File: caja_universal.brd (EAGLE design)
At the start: 136.8 x 101.5 mm, 39 parts, among them IC1 AD711N, IC2 AD620N, IC3 TL084P, IC4 TL084P, IC5 AD711N

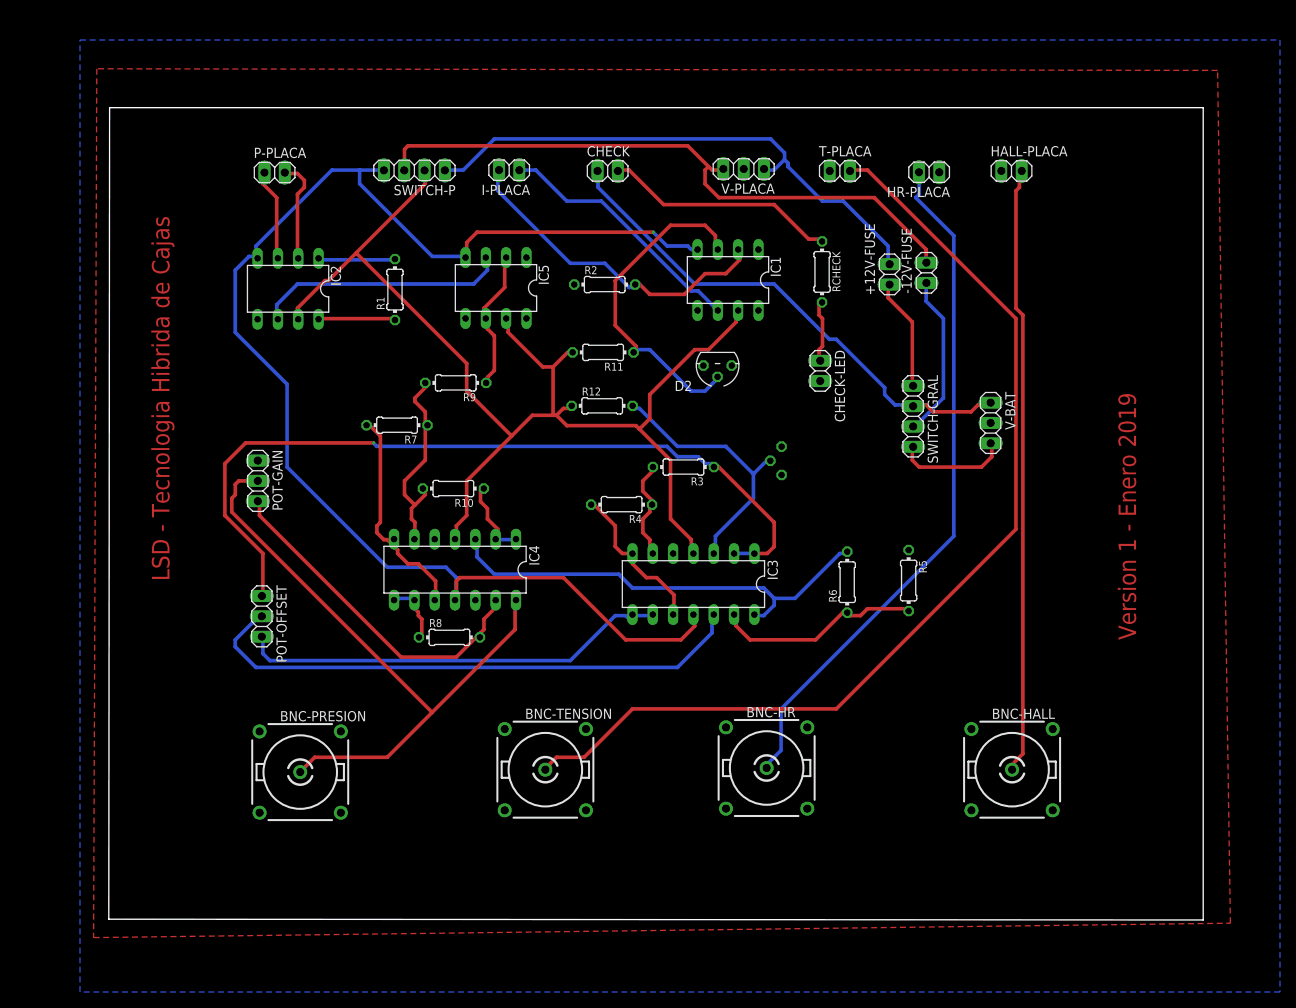
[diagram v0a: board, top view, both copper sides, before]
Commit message: Nuevo circuito de sense
Agrego circuito diseñado por Gonza para no tener que usar los cables de check
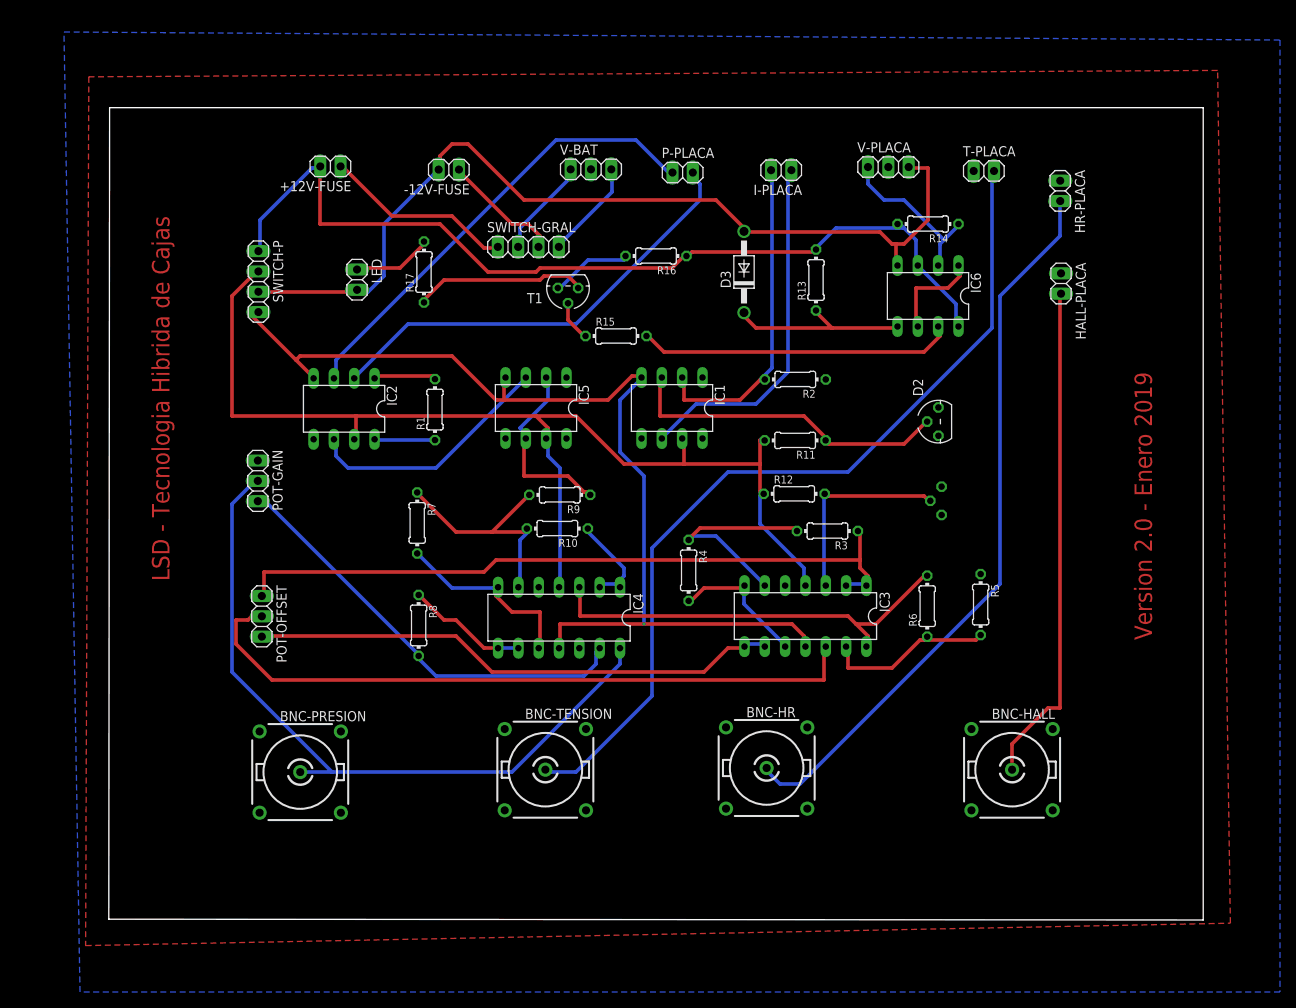
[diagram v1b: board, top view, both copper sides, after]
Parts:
- removed CHECK, CHECK-LED: (no value), pinhead:1X02
- removed RCHECK: 100k, resistor:0204/7
- added D3: BAT49, diode:DO41-10
- added IC6: AD826N, analog-devices:DIL08
- added LED: (no value), pinhead:1X02
- added R13, R15: 100k, resistor:0204/7
- added R14: 10, resistor:0204/7
- added R16, R17: 10k, resistor:0204/7
- added T1: 2N3904, transistor:TO92
- moved +12V-FUSE 71.2 mm to (9.30, 81.2), turned to 180 degrees
- moved -12V-FUSE 61.1 mm to (24.1, 80.8), turned to 180 degrees
- moved V-BAT 59.2 mm to (41.9, 80.8), turned to 0 degrees
- moved SWITCH-GRAL 52.6 mm to (34.0, 71.1), turned to 0 degrees
- moved P-PLACA 51.0 mm to (53.3, 80.4)
- moved I-PLACA 34.0 mm to (65.7, 80.7)
- moved D2 28.5 mm to (85.3, 49.3), turned to 90 degrees
- moved R2 26.6 mm to (67.4, 54.6), turned to 180 degrees
- moved R11 26.4 mm to (67.4, 47.0)
- moved R12 26.4 mm to (67.3, 40.3)
- moved SWITCH-P 23.9 mm to (0.30, 66.8), turned to 270 degrees
- moved D1 20.6 mm to (85.7, 39.4)
- moved R3 19.7 mm to (71.4, 35.6)
- moved R9 19.1 mm to (38.0, 40.1)
- moved V-PLACA 18.1 mm to (79.0, 81.1), turned to 0 degrees
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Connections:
- removed net N$1: CHECK-LED.1, RCHECK.2
- removed net N$2: CHECK.2, RCHECK.1
- new net +12VPLACA: IC6.2, R14.1, V-PLACA.1
- new net CHECK-LED: LED.1, R17.2
- new net N$17: R15.1, T1.2
- new net N$18: R16.2, T1.1
- new net N$19: R17.1, T1.3
- new net N$21: IC6.1, IC6.6
- new net N$23: D3.C, IC6.5, R13.1
- new net N$24: IC6.7, R15.2
- net +12V: now also IC6.3, IC6.8, R13.2, R14.2, R16.1; no longer V-PLACA.1
- net +12VBAT: no longer CHECK.1
- net -12V: now also D3.A, IC6.4, LED.2
- net 0V: no longer CHECK-LED.2
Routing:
- net +12VBAT: track 63.9 -> 12.4 mm
- net +12V: track 68.8 -> 115.7 mm
- net P+: track 11.6 -> 58.1 mm
- net P-: track 12.9 -> 56.3 mm
- net V-: track 170.7 -> 130.9 mm
- net N$24: track 0.00 -> 39.6 mm
- net -12V: track 79.0 -> 114.7 mm
- net N$2: track 29.3 -> 0.00 mm
- net N$23: track 0.00 -> 23.3 mm
- net N$19: track 0.00 -> 21.9 mm
- net +12VPLACA: track 0.00 -> 21.0 mm
- net TENSION: track 126.6 -> 109.5 mm
- net OFFSET: track 70.3 -> 86.1 mm
- net N$6: track 13.3 -> 26.8 mm
- net HALL: track 76.4 -> 62.9 mm
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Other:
- board text added: "Version 2.0 - Enero 2019"
- board text removed: "Version 1 - Enero 2019"

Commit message: Version 2.1
Smasheo todo para que los nombres y valores de todos los componentes queden visibles

Cambio los nombres de los integrados para que sean los que usamos
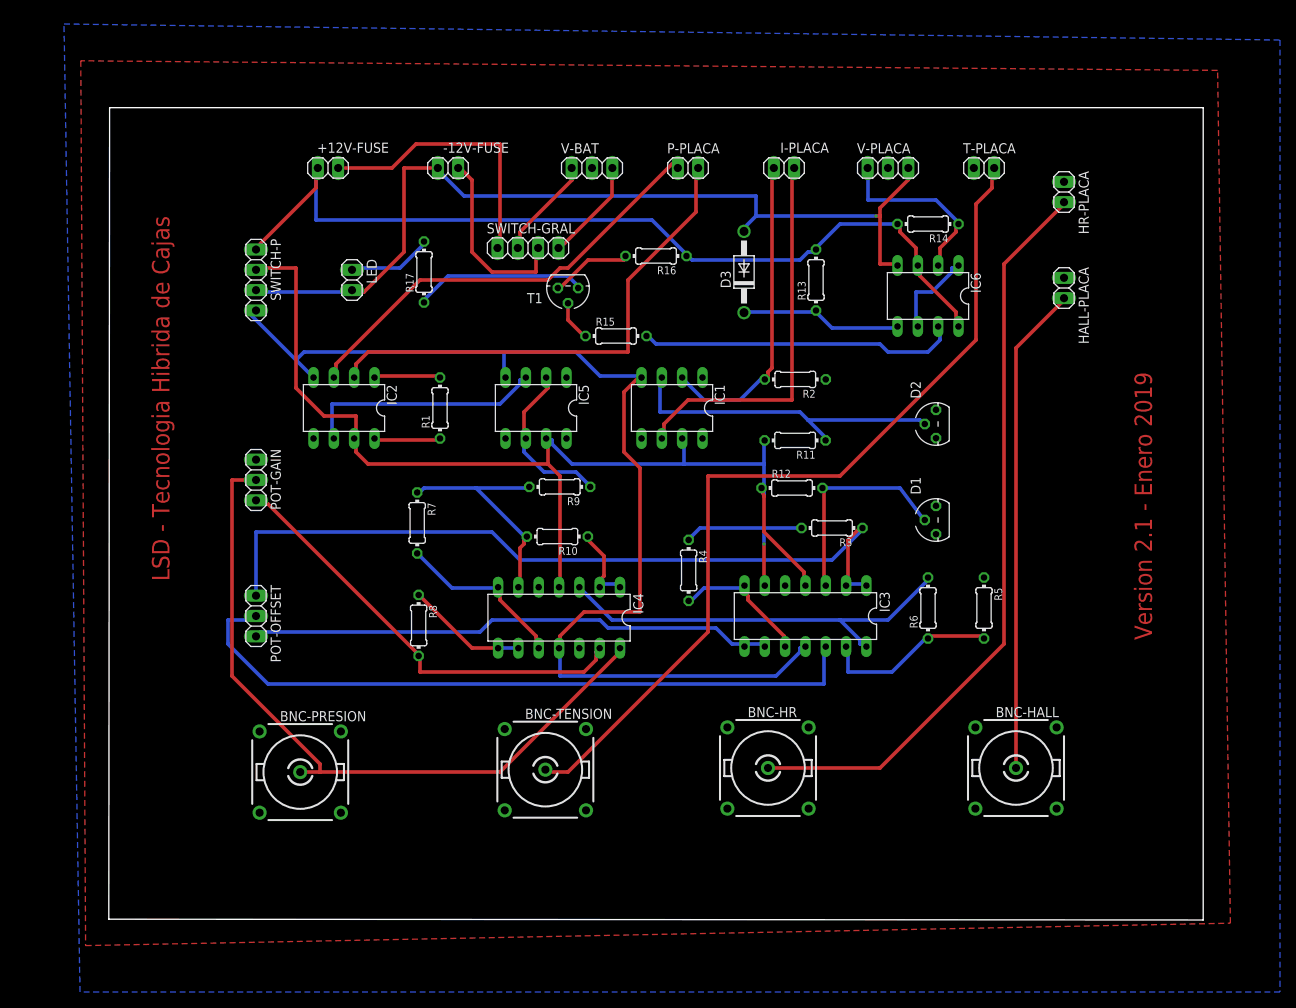
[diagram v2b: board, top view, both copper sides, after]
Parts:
- IC1, IC5: value AD711N -> NE5534
- IC6: value AD826N -> TL072
- moved D1 2.50 mm to (85.0, 37.0), flipped to the top, turned to 90 degrees
- moved R10 1.00 mm to (37.7, 34.9)
- moved R9 1.00 mm to (38.0, 41.1)
- moved P-PLACA 0.88 mm to (54.0, 81.0)
- moved R12 0.78 mm to (67.0, 41.0)
- moved POT-OFFSET 0.73 mm to (0.00, 25.0)
- moved R3 0.69 mm to (72.0, 36.0)
- moved HALL-PLACA 0.67 mm to (101.0, 66.0)
- moved R1 0.66 mm to (23.0, 51.0)
- moved LED 0.63 mm to (12.0, 67.0)
- moved R5 0.60 mm to (91.0, 26.0)
- moved BNC-HALL 0.53 mm to (95.0, 6.00)
- moved HR-PLACA 0.49 mm to (101.0, 78.0)
- moved I-PLACA 0.44 mm to (66.0, 81.0)
- moved D2 0.42 mm to (85.0, 49.0)
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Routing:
- net +12VFUSE: track 23.9 -> 34.8 mm
- net V-: track 130.9 -> 140.5 mm, vias 1 -> 0
- net 1.25V: track 88.5 -> 98.2 mm
- net -12VFUSE: track 15.0 -> 23.7 mm
- net P-: track 56.3 -> 63.2 mm
- net V+: track 138.8 -> 132.3 mm
- net N$6: track 26.8 -> 22.0 mm, vias 0 -> 1
- net +I: track 44.7 -> 48.4 mm
- net N$23: track 23.3 -> 20.4 mm
- net N$13: track 23.7 -> 20.9 mm
- net P+: track 58.1 -> 55.4 mm
- net N$9: track 13.2 -> 10.7 mm
- net +12VPLACA: track 21.0 -> 23.4 mm
- net N$14: track 24.2 -> 21.9 mm
- net HR: track 92.0 -> 94.3 mm
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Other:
- board text added: "Version 2.1 - Enero 2019"
- board text removed: "Version 2.0 - Enero 2019"

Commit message: Corregidos valores circuito sense, potenciometro gain y cambio de libreria conectores. Agrego tRestrict alrededor de conectores para que las vias salgan siempre de bottom
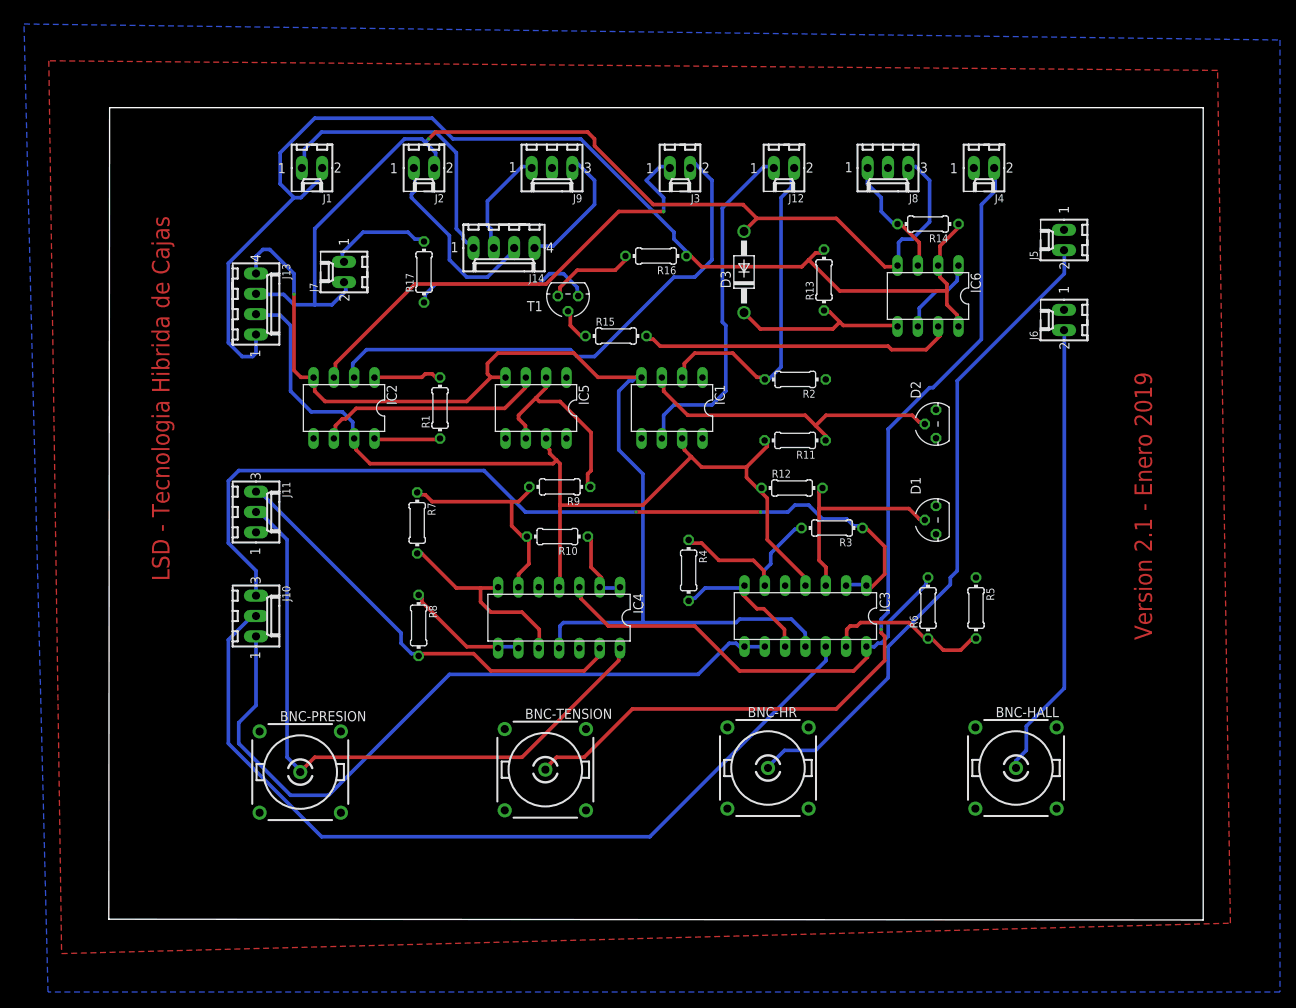
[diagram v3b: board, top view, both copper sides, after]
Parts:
- removed +12V-FUSE, -12V-FUSE, HALL-PLACA, HR-PLACA, I-PLACA, LED, P-PLACA, T-PLACA: (no value), pinhead:1X02
- removed POT-GAIN, POT-OFFSET, V-BAT, V-PLACA: (no value), pinhead:1X03
- removed SWITCH-GRAL, SWITCH-P: (no value), pinhead:1X04
- added J1: +12V-FUSE, con-molex:6410-02
- added J10: POT-OFFSET, con-molex:6410-03
- added J11: POT-GAIN, con-molex:6410-03
- added J12: I-PLACA, con-molex:6410-02
- added J13: SWITCH-P, con-molex:6410-04
- added J14: SWITCH-GRAL, con-molex:6410-04
- added J2: -12V-FUSE, con-molex:6410-02
- added J3: P-PLACA, con-molex:6410-02
- added J4: T-PLACA, con-molex:6410-02
- added J5: HR-PLACA, con-molex:6410-02
- added J6: HALL-PLACA, con-molex:6410-02
- added J7: LED, con-molex:6410-02
- added J8: V-PLACA, con-molex:6410-03
- added J9: V-BAT, con-molex:6410-03
- R16, R17: value 10k -> 1k
- moved R13 1.00 mm to (71.0, 67.0)
- moved R5 1.00 mm to (90.0, 26.0)
- moved T1 1.00 mm to (39.0, 65.0)
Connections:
- net +12V: now also IC6.2, J1.2, J13.1, R14.1; no longer +12V-FUSE.2, IC6.3, R14.2, SWITCH-P.1
- net +12VBAT: now also J14.2, J9.1; no longer SWITCH-GRAL.2, V-BAT.1
- net +12VFUSE: now also J1.1, J14.1; no longer +12V-FUSE.1, SWITCH-GRAL.1
- net +12VPLACA: now also IC6.3, J8.1, R14.2; no longer IC6.2, R14.1, V-PLACA.1
- net +I: now also J12.1; no longer I-PLACA.1
- net -1.25V: now also J10.1; no longer POT-OFFSET.3
- net -12V: now also J13.3, J2.2, J7.2, J8.3; no longer -12V-FUSE.2, LED.2, SWITCH-P.3, V-PLACA.3
- net -12VBAT: now also J14.4, J9.3; no longer SWITCH-GRAL.4, V-BAT.3
- net -12VFUSE: now also J14.3, J2.1; no longer -12V-FUSE.1, SWITCH-GRAL.3
- net -I: now also J12.2; no longer I-PLACA.2
- net 0V: now also J8.2, J9.2; no longer POT-GAIN.1, V-BAT.2, V-PLACA.2
- net 1.25V: now also J10.3; no longer POT-OFFSET.1
- net CHECK-LED: now also J7.1; no longer LED.1
- net HALL: now also J6.2; no longer HALL-PLACA.2
- net HR: now also J5.2; no longer HR-PLACA.2
- net N$16: now also J11.3; no longer POT-GAIN.3
- net OFFSET: now also J10.2; no longer POT-OFFSET.2
- net P+: now also J3.1; no longer P-PLACA.1
- net P-: now also J3.2; no longer P-PLACA.2
- net POUT: now also J11.2; no longer POT-GAIN.2
- net TENSION: now also J4.2; no longer T-PLACA.2
- net V+: now also J13.2; no longer SWITCH-P.2
- net V-: now also J13.4; no longer SWITCH-P.4
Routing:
- net +12V: track 113.5 -> 153.7 mm
- net -1.25V: track 66.3 -> 91.4 mm
- net OFFSET: track 88.1 -> 108.3 mm
- net -12V: track 114.0 -> 131.6 mm
- net 1.25V: track 98.2 -> 113.2 mm, vias 0 -> 2
- net HR: track 94.3 -> 82.4 mm
- net V+: track 132.3 -> 123.5 mm
- net POUT: track 90.7 -> 83.0 mm
- net +12VPLACA: track 23.4 -> 15.8 mm
- net TENSION: track 110.3 -> 116.4 mm, vias 0 -> 1
- net +I: track 48.4 -> 43.7 mm
- net N$13: track 20.9 -> 25.2 mm
- net -12VBAT: track 12.9 -> 17.2 mm
- net P-: track 63.2 -> 67.3 mm
- net HALL: track 61.2 -> 57.2 mm
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
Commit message: Agrego tRestrict alrededor de todos los zocalos
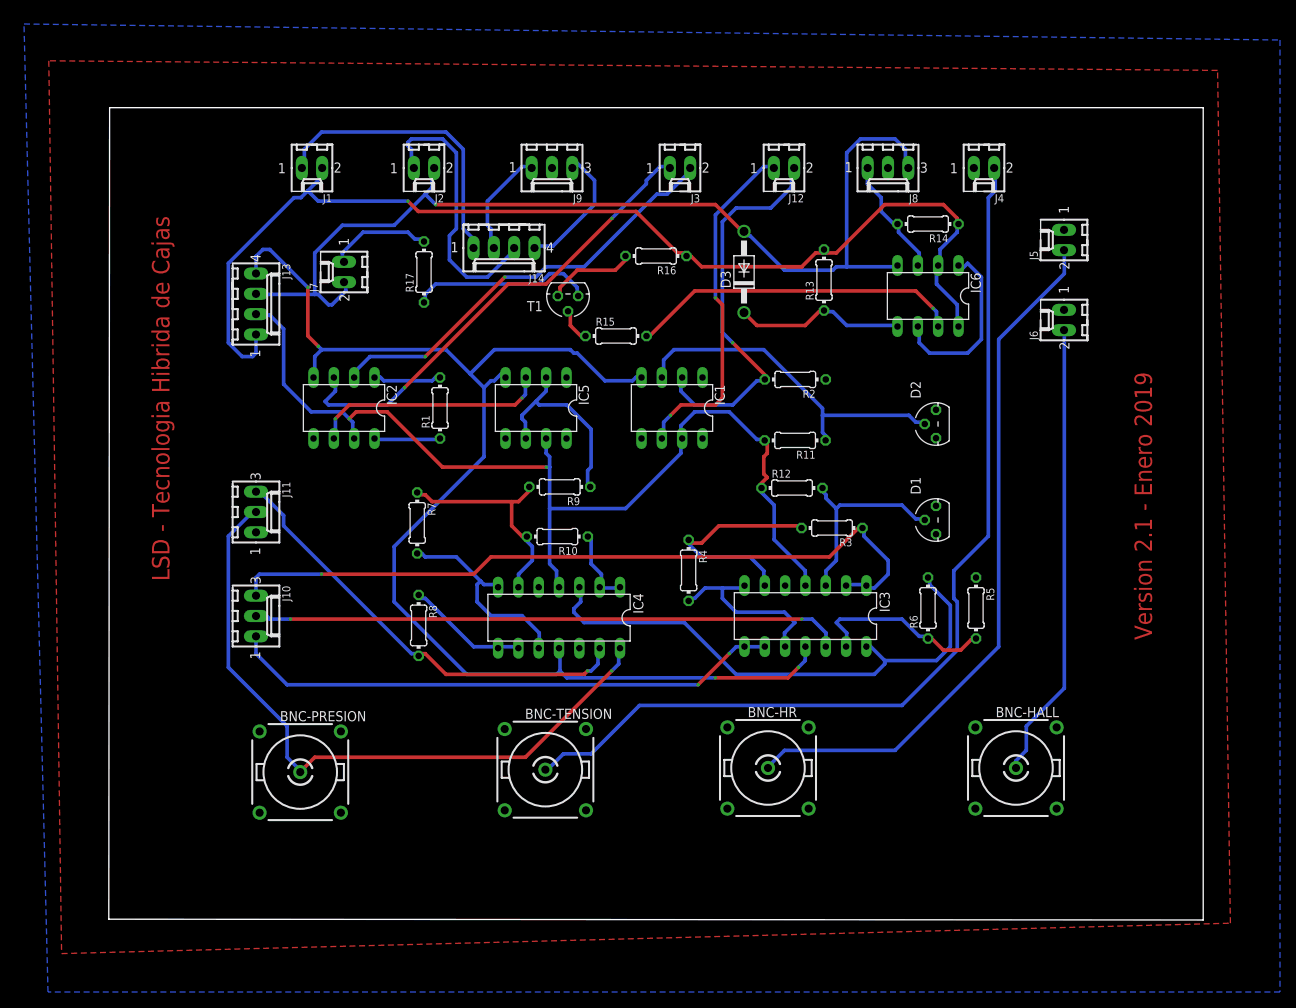
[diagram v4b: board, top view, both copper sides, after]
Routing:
- net OFFSET: track 108.3 -> 73.9 mm, vias 0 -> 2
- net V-: track 144.4 -> 167.0 mm, vias 1 -> 4
- net -1.25V: track 91.4 -> 69.3 mm, vias 0 -> 2
- net 1.25V: track 113.2 -> 94.3 mm, vias 2 -> 1
- net +12V: track 153.7 -> 139.3 mm, vias 0 -> 1
- net P-: track 67.3 -> 53.7 mm, vias 0 -> 2
- net N$11: track 56.0 -> 68.9 mm
- net N$21: track 10.5 -> 23.4 mm
- net -12VFUSE: track 24.4 -> 35.0 mm
- net -I: track 42.4 -> 49.4 mm, vias 0 -> 1
- net N$6: track 22.5 -> 28.5 mm
- net HR: track 82.4 -> 88.3 mm
- net V+: track 123.5 -> 128.4 mm, vias 0 -> 2
- net N$8: track 18.1 -> 23.0 mm
- net TENSION: track 116.4 -> 120.5 mm, vias 1 -> 0
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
